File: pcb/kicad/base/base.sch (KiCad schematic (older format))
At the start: 37 parts, among them J1 CHIP_EN, J2 Vbatt_I-test, P1 J-Link SWD, P2 SMA, P3 Power Source, P4 CONN_01X08, U1 SAMB11G18A-edit, Y1 32.768kHz, Y2 26MHz

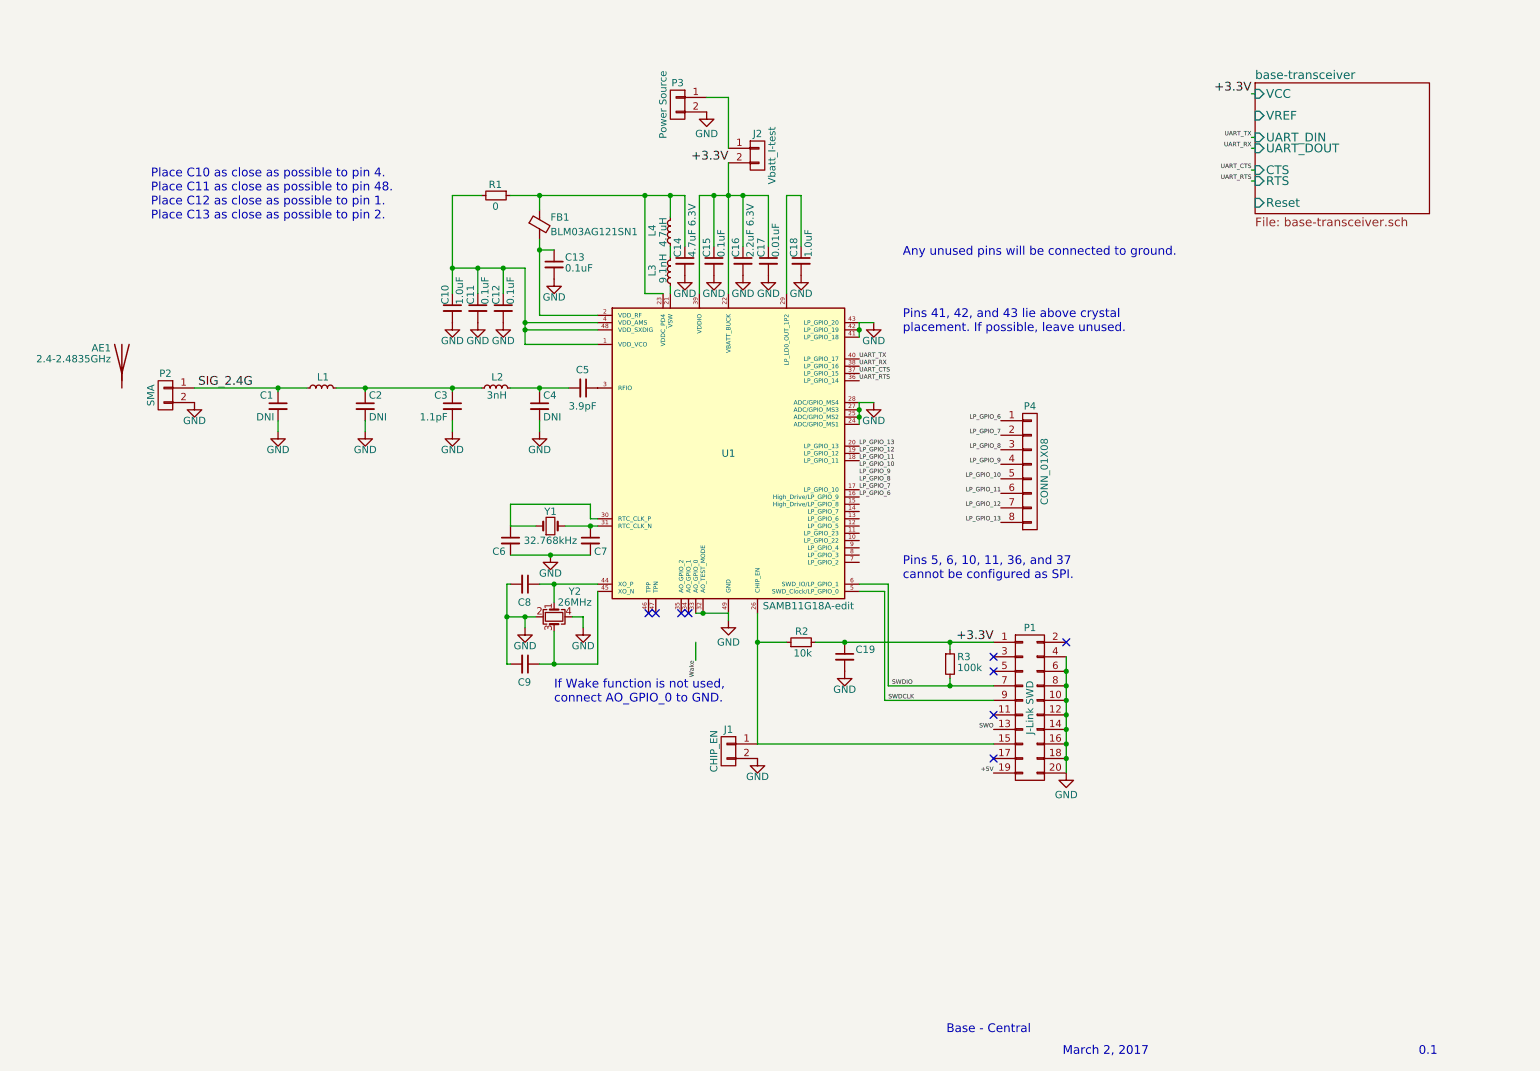
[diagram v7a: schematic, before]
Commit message: Add 16x4 LCD display symbol
Symbol and schematic started for the Crystalfontz display to be used
for user interface. Display contrast and LCD brightness settings need
to configured based on breadboard testing. Layout will be reworked to
properly accompany the mass pin usage of the display.
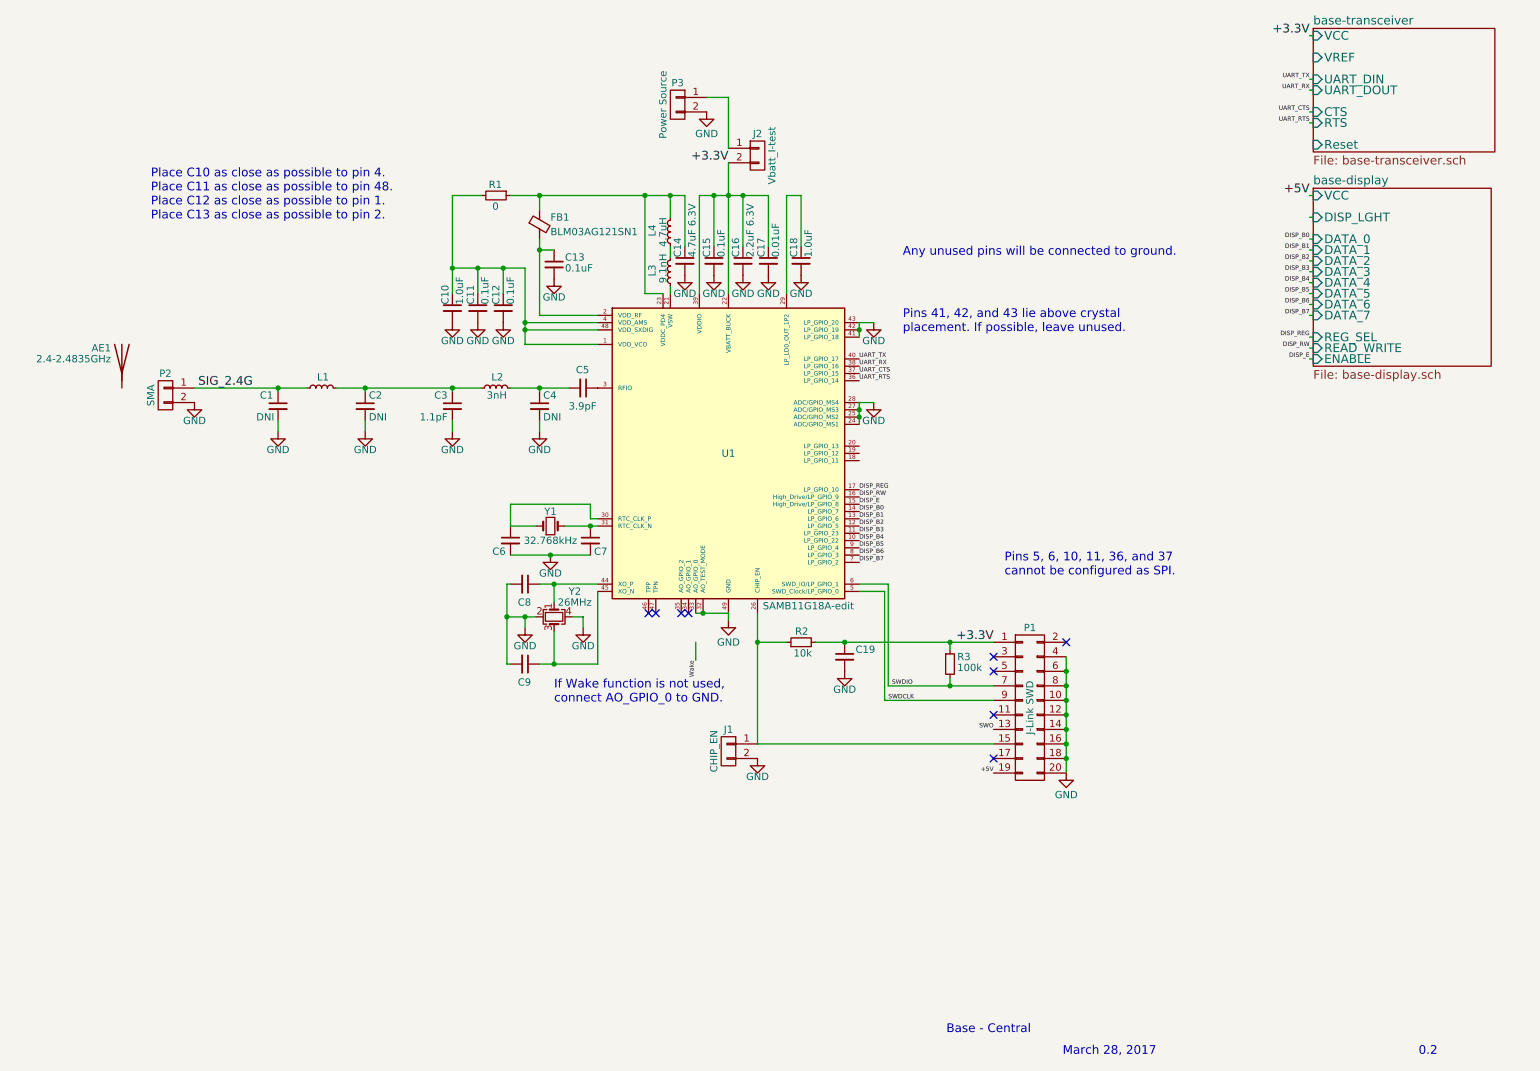
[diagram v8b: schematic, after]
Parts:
- removed P4: CONN_01X08, Misc:Socket_Strip_Straight_1x08_Pitch2.54mm_Drill0.64mm, symbol CONN_01X08
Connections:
- net DISP_B4: now reaches U1.10 (LP_GPIO_22)
- net DISP_B3: now reaches U1.11 (LP_GPIO_23)
- net DISP_B2: now reaches U1.12 (LP_GPIO_5)
- net DISP_B1: now reaches U1.13 (LP_GPIO_6)
- net DISP_B0: now reaches U1.14 (LP_GPIO_7)
- net DISP_E: now reaches U1.15 (High_Drive/LP_GPIO_8)
- net DISP_B7: now reaches U1.7 (LP_GPIO_2)
- net DISP_B6: now reaches U1.8 (LP_GPIO_3)
- net DISP_B5: now reaches U1.9 (LP_GPIO_4)
- net LP_GPIO_11: no longer names the net of U1.18 (LP_GPIO_11)
- net LP_GPIO_12: no longer names the net of U1.19 (LP_GPIO_12)
- net LP_GPIO_13: no longer names the net of U1.20 (LP_GPIO_13)
- net LP_GPIO_6 renamed DISP_RW
- net LP_GPIO_7 renamed DISP_REG
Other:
- note added: "0.2"
- note added: "March 28, 2017"
- note removed: "0.1"
- note removed: "March 2, 2017"
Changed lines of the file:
@@
 LIBS:valves
 LIBS:rf_transceivers
+LIBS:displays
 LIBS:base-cache
 EELAYER 25 0
@@
 $Descr A4 11693 8268
 encoding utf-8
-Sheet 1 2
+Sheet 1 3
 Title ""
 Date ""
@@
 Base - Central
 Text Notes 8150 7650 0    60   ~ 0
-March 2, 2017
+March 28, 2017
 Text Notes 10600 7650 0    60   ~ 0
-0.1
+0.2
 $Comp
 L GND #PWR01
@@
 Text Label 6750 2950 0    30   ~ 0
 UART_CTS
-Text Label 6750 3700 0    30   ~ 0
-LP_GPIO_8
-Text Label 6750 3650 0    30   ~ 0
-LP_GPIO_9
+Text Label 6750 4150 0    30   ~ 0
+DISP_B5
+Text Label 6750 4100 0    30   ~ 0
+DISP_B4
 Text Label 5625 4925 3    30   ~ 0
 Wake
@@
 If Wake function is not used,\nconnect AO_GPIO_0 to GND.
 $Sheet
-S 9475 950  1200 900
+S 9875 575  1250 850
 U 58C0BD85
 F0 "base-transceiver" 60
 F1 "base-transceiver.sch" 60
-F2 "VCC" I L 9475 1025 60
-F3 "Reset" I L 9475 1775 60
-F4 "VREF" I L 9475 1175 60
-F5 "CTS" I L 9475 1550 60
-F6 "RTS" I L 9475 1625 60
-F7 "UART_DIN" I L 9475 1325 60
-F8 "UART_DOUT" I L 9475 1400 60
+F2 "VCC" I L 9875 625 60
+F3 "Reset" I L 9875 1375 60
+F4 "VREF" I L 9875 775 60
+F5 "CTS" I L 9875 1150 60
+F6 "RTS" I L 9875 1225 60
+F7 "UART_DIN" I L 9875 925 60
+F8 "UART_DOUT" I L 9875 1000 60
 $EndSheet
-Text Label 9450 1025 2    60   ~ 0
+Text Label 9850 625  2    60   ~ 0
 +3.3V
-Text Label 9450 1625 2    30   ~ 0
+Text Label 9850 1225 2    30   ~ 0
 UART_RTS
-Text Label 9450 1550 2    30   ~ 0
+Text Label 9850 1150 2    30   ~ 0
 UART_CTS
-Text Label 9450 1325 2    30   ~ 0
+Text Label 9850 925  2    30   ~ 0
 UART_TX
-Text Label 9450 1400 2    30   ~ 0
+Text Label 9850 1000 2    30   ~ 0
 UART_RX
 $Comp
@@
 Text Label 6750 2900 0    30   ~ 0
 UART_RX
-Text Label 6750 3450 0    30   ~ 0
-LP_GPIO_13
-Text Label 6750 3500 0    30   ~ 0
-LP_GPIO_12
-Text Label 6750 3550 0    30   ~ 0
-LP_GPIO_11
-Text Label 6750 3600 0    30   ~ 0
-LP_GPIO_10
-Text Label 6750 3750 0    30   ~ 0
-LP_GPIO_7
-Text Label 6750 3800 0    30   ~ 0
-LP_GPIO_6
+Text Label 6750 3900 0    30   ~ 0
+DISP_B0
+Text Label 6750 3950 0    30   ~ 0
+DISP_B1
+Text Label 6750 4000 0    30   ~ 0
+DISP_B2
+Text Label 6750 4050 0    30   ~ 0
+DISP_B3
+Text Label 6750 4200 0    30   ~ 0
+DISP_B6
+Text Label 6750 4250 0    30   ~ 0
+DISP_B7
 $Comp
 L GND #PWR023
@@
 $EndComp
 $Comp
-L CONN_01X08 P4
-U 1 1 58C384E9
-P 7925 3625
-F 0 "P4" H 7925 4075 50  0000 C CNN
-F 1 "CONN_01X08" V 8025 3625 50  0000 C CNN
-F 2 "Misc:Socket_Strip_Straight_1x08_Pitch2.54mm_Drill0.64mm" H 7925 3625 50  0001 C CNN
-F 3 "" H 7925 3625 50  0000 C CNN
-	1    7925 3625
-	1    0    0    -1
-$EndComp
-Text Label 7725 3275 2    30   ~ 0
-LP_GPIO_6
-Text Label 7725 3375 2    30   ~ 0
-LP_GPIO_7
-Text Label 7725 3475 2    30   ~ 0
-LP_GPIO_8
-Text Label 7725 3575 2    30   ~ 0
-LP_GPIO_9
-Text Label 7725 3675 2    30   ~ 0
-LP_GPIO_10
-Text Label 7725 3775 2    30   ~ 0
-LP_GPIO_11
-Text Label 7725 3875 2    30   ~ 0
-LP_GPIO_12
-Text Label 7725 3975 2    30   ~ 0
-LP_GPIO_13
-$Comp
 L SAMB11G18A-edit U1
 U 1 1 58C5ED8B
@@
 $EndComp
 $Comp
-L GND #PWR?
+L GND #PWR024
 U 1 1 58C65889
 P 6850 2600
-F 0 "#PWR?" H 6850 2350 50  0001 C CNN
+F 0 "#PWR024" H 6850 2350 50  0001 C CNN
 F 1 "GND" H 6850 2475 50  0000 C CNN
 F 2 "" H 6850 2600 50  0000 C CNN
@@
 	1    0    0    -1
 $EndComp
+Text Notes 7050 2675 0    60   ~ 0
+Pins 41, 42, and 43 lie above crystal\nplacement. If possible, leave unused.
+Text Notes 7050 2150 0    60   ~ 0
+Any unused pins will be connected to ground.
 Wire Wire Line
 	3150 3050 4150 3050
@@
 	6050 5500 7675 5500
 Wire Wire Line
-	9475 1025 9450 1025
-Wire Wire Line
-	9475 1325 9450 1325
-Wire Wire Line
-	9475 1400 9450 1400
-Wire Wire Line
-	9475 1550 9450 1550
-Wire Wire Line
-	9475 1625 9450 1625
+	9875 625  9850 625
+Wire Wire Line
+	9875 925  9850 925
+Wire Wire Line
+	9875 1000 9850 1000
+Wire Wire Line
+	9875 1150 9850 1150
+Wire Wire Line
+	9875 1225 9850 1225
 Wire Wire Line
 	4775 4625 4850 4625
@@
 Wire Wire Line
 	6750 2600 6850 2600
-Text Notes 7050 2675 0    60   ~ 0
-Pins 41, 42, and 43 lie above crystal\nplacement. If possible, leave unused.
-Text Notes 7050 2150 0    60   ~ 0
-Any unused pins will be connected to ground.
-Text Notes 7050 4375 0    60   ~ 0
+Wire Wire Line
+	9875 1725 9850 1725
+Wire Wire Line
+	9875 1875 9850 1875
+Wire Wire Line
+	9875 2025 9850 2025
+Wire Wire Line
+	9875 2100 9850 2100
+Wire Wire Line
+	9875 2175 9850 2175
+Wire Wire Line
+	9875 2250 9850 2250
+Wire Wire Line
+	9875 2325 9850 2325
+Wire Wire Line
+	9875 2400 9850 2400
+Wire Wire Line
+	9875 2475 9850 2475
+Wire Wire Line
+	9875 2550 9850 2550
+Wire Wire Line
+	9875 2700 9850 2700
+Wire Wire Line
+	9875 2775 9850 2775
+$Sheet
+S 9875 1675 1225 1225
+U 58DB875D
+F0 "base-display" 60
+F1 "base-display.sch" 60
+F2 "DATA_0" I L 9875 2025 60
+F3 "DATA_1" I L 9875 2100 60
+F4 "DATA_2" I L 9875 2175 60
+F5 "DATA_3" I L 9875 2250 60
+F6 "DATA_4" I L 9875 2325 60
+F7 "DATA_5" I L 9875 2400 60
+F8 "DATA_6" I L 9875 2475 60
+F9 "REG_SEL" I L 9875 2700 60
+F10 "READ_WRITE" I L 9875 2775 60
+F11 "ENABLE" I L 9875 2850 60
+F12 "VCC" I L 9875 1725 60
+F13 "DISP_LGHT" I L 9875 1875 60
+F14 "DATA_7" I L 9875 2550 60
+$EndSheet
+Text Notes 7750 4350 0    60   ~ 0
 Pins 5, 6, 10, 11, 36, and 37\ncannot be configured as SPI.\n
+Text Label 9850 1725 2    60   ~ 0
++5V
+Text Label 9850 2025 2    30   ~ 0
+DISP_B0
+Text Label 9850 2100 2    30   ~ 0
+DISP_B1
+Text Label 9850 2175 2    30   ~ 0
+DISP_B2
+Text Label 9850 2250 2    30   ~ 0
+DISP_B3
+Text Label 9850 2325 2    30   ~ 0
+DISP_B4
+Text Label 9850 2400 2    30   ~ 0
+DISP_B5
+Text Label 9850 2475 2    30   ~ 0
+DISP_B6
+Text Label 9850 2550 2    30   ~ 0
+DISP_B7
+Wire Wire Line
+	9850 2850 9875 2850
+Text Label 9850 2700 2    30   ~ 0
+DISP_REG
+Text Label 9850 2775 2    30   ~ 0
+DISP_RW
+Text Label 9850 2850 2    30   ~ 0
+DISP_E
+Text Label 6750 3850 0    30   ~ 0
+DISP_E
+Text Label 6750 3800 0    30   ~ 0
+DISP_RW
+Text Label 6750 3750 0    30   ~ 0
+DISP_REG
 $EndSCHEMATC
